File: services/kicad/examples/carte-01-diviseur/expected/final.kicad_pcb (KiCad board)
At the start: 2 copper layers, 25 x 20 mm, 5 parts, among them J1 IN

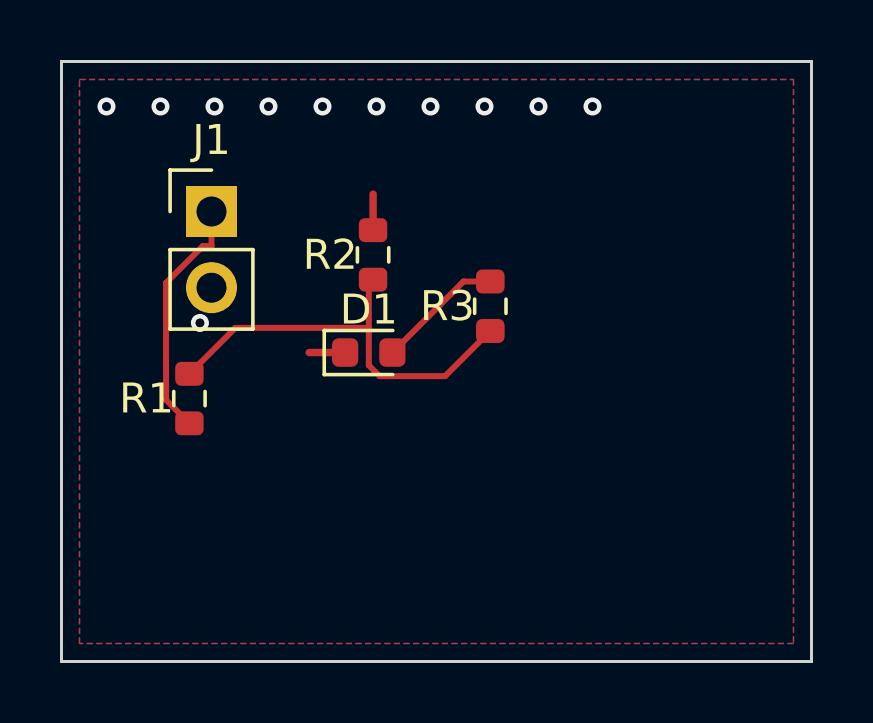
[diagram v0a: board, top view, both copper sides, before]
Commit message: test(examples): banc regenere -- placements livres, journaux et mesures a jour
- expected/placement.kicad_pcb ajoutes (carte-05, carte-06) et
  vue-dessus.png (carte-04) : le banc compare desormais le placement,
  pas seulement le board final.
- generer_exemples.py, regenerer_le_banc.py, livrer_placements.py,
  apercu_routage.py : regeneration reproductible du banc et rendus
  d apercu.
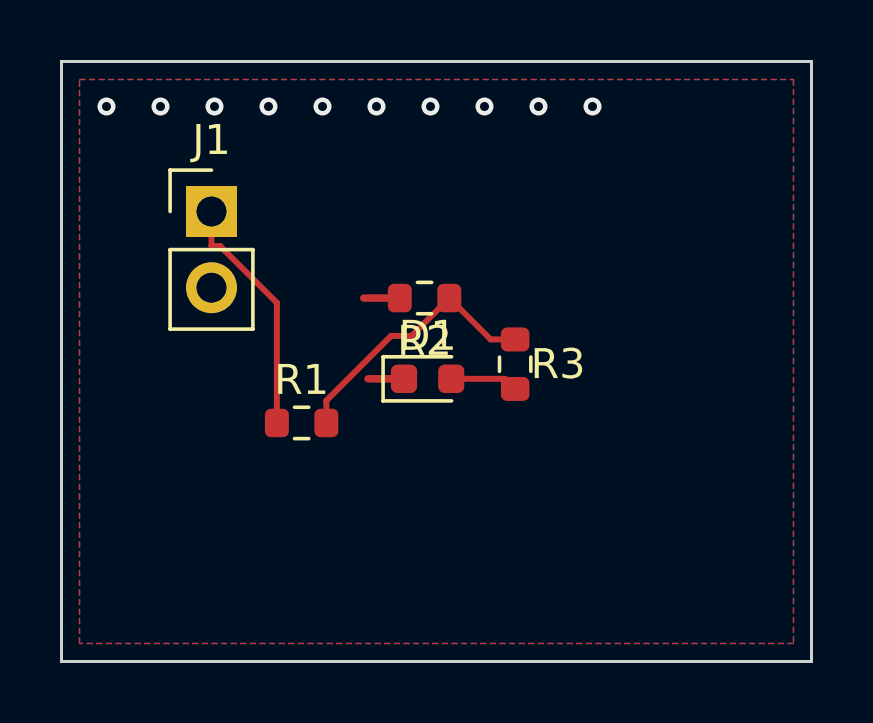
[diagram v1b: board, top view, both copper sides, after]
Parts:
- moved R1 3.83 mm to (144.0, 107.0), turned to 0 degrees
- moved R2 2.24 mm to (148.1, 102.9), turned to 180 degrees
- moved D1 2.15 mm to (148.2, 105.6)
- moved R3 2.10 mm to (151.1, 105.1), turned to -90 degrees
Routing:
- net MID: track 14.4 -> 9.02 mm
- net LED_A: track 4.24 -> 2.27 mm
- net GND: vias 11 -> 10
